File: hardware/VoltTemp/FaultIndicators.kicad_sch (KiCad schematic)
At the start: 16 parts

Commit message: layout
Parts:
- D2, D3, D4, D5, D6, D7, D8, D9: footprint LED_SMD:LED_WS2812B_PLCC4_5.0x5.0mm_P3.2mm -> LED_SMD:LED_WS2812B-2020_PLCC4_2.0x2.0mm
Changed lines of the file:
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@@
 			)
 		)
-		(property "Footprint" "LED_SMD:LED_WS2812B_PLCC4_5.0x5.0mm_P3.2mm"
+		(property "Footprint" "LED_SMD:LED_WS2812B-2020_PLCC4_2.0x2.0mm"
 			(at 120.65 60.96 0)
 			(effects
@@
 			)
 		)
-		(property "Footprint" "LED_SMD:LED_WS2812B_PLCC4_5.0x5.0mm_P3.2mm"
+		(property "Footprint" "LED_SMD:LED_WS2812B-2020_PLCC4_2.0x2.0mm"
 			(at 191.77 60.96 0)
 			(effects
@@
 			)
 		)
-		(property "Footprint" "LED_SMD:LED_WS2812B_PLCC4_5.0x5.0mm_P3.2mm"
+		(property "Footprint" "LED_SMD:LED_WS2812B-2020_PLCC4_2.0x2.0mm"
 			(at 156.21 104.14 0)
 			(effects
@@
 			)
 		)
-		(property "Footprint" "LED_SMD:LED_WS2812B_PLCC4_5.0x5.0mm_P3.2mm"
+		(property "Footprint" "LED_SMD:LED_WS2812B-2020_PLCC4_2.0x2.0mm"
 			(at 85.09 104.14 0)
 			(effects
@@
 			)
 		)
-		(property "Footprint" "LED_SMD:LED_WS2812B_PLCC4_5.0x5.0mm_P3.2mm"
+		(property "Footprint" "LED_SMD:LED_WS2812B-2020_PLCC4_2.0x2.0mm"
 			(at 85.09 60.96 0)
 			(effects
@@
 			)
 		)
-		(property "Footprint" "LED_SMD:LED_WS2812B_PLCC4_5.0x5.0mm_P3.2mm"
+		(property "Footprint" "LED_SMD:LED_WS2812B-2020_PLCC4_2.0x2.0mm"
 			(at 120.65 104.14 0)
 			(effects
@@
 			)
 		)
-		(property "Footprint" "LED_SMD:LED_WS2812B_PLCC4_5.0x5.0mm_P3.2mm"
+		(property "Footprint" "LED_SMD:LED_WS2812B-2020_PLCC4_2.0x2.0mm"
 			(at 191.77 104.14 0)
 			(effects
@@
 			)
 		)
-		(property "Footprint" "LED_SMD:LED_WS2812B_PLCC4_5.0x5.0mm_P3.2mm"
+		(property "Footprint" "LED_SMD:LED_WS2812B-2020_PLCC4_2.0x2.0mm"
 			(at 156.21 60.96 0)
 			(effects

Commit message: layout2 electric boogaloo
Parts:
- removed D2, D3, D4, D5, D6, D7, D8, D9: WS2812B, LED_SMD:LED_WS2812B-2020_PLCC4_2.0x2.0mm, symbol LED:WS2812B
- added D2, D3, D4, D5, D6, D7, D8, D9: WS2812B-2020, LED_SMD:LED_WS2812B-2020_PLCC4_2.0x2.0mm, symbol LED:WS2812B-2020
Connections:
- net +3V3: now also D2.4 (VDD), D3.4 (VDD), D4.4 (VDD), D5.4 (VDD), D6.4 (VDD), D7.4 (VDD), D8.4 (VDD), D9.4 (VDD)
- net GND: now also D2.2 (VSS), D3.2 (VSS), D4.2 (VSS), D5.2 (VSS), D6.2 (VSS), D7.2 (VSS), D8.2 (VSS), D9.2 (VSS)
- net LedDin: now also D2.3 (DIN)
- new net: D3.1 (DOUT), D4.3 (DIN)
- new net: D2.1 (DOUT), D3.3 (DIN)
- new net: D4.1 (DOUT), D5.3 (DIN)
- new net: D7.1 (DOUT), D8.3 (DIN)
- new net: D6.1 (DOUT), D7.3 (DIN)
- new net: D8.1 (DOUT), D9.3 (DIN)
- new net: D5.1 (DOUT), D6.3 (DIN)

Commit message: add thermistor test board, just need to route volttemp testpoints
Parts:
- D2, D3, D4, D5, D6, D7, D8, D9: footprint LED_SMD:LED_WS2812B-2020_PLCC4_2.0x2.0mm -> VoltTemp:WS2812B-2020
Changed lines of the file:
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@@
 			)
 		)
-		(property "Footprint" "LED_SMD:LED_WS2812B-2020_PLCC4_2.0x2.0mm"
+		(property "Footprint" "VoltTemp:WS2812B-2020"
 			(at 120.65 60.96 0)
 			(effects
@@
 			)
 		)
-		(property "Footprint" "LED_SMD:LED_WS2812B-2020_PLCC4_2.0x2.0mm"
+		(property "Footprint" "VoltTemp:WS2812B-2020"
 			(at 85.09 60.96 0)
 			(effects
@@
 			)
 		)
-		(property "Footprint" "LED_SMD:LED_WS2812B-2020_PLCC4_2.0x2.0mm"
+		(property "Footprint" "VoltTemp:WS2812B-2020"
 			(at 156.21 60.96 0)
 			(effects
@@
 			)
 		)
-		(property "Footprint" "LED_SMD:LED_WS2812B-2020_PLCC4_2.0x2.0mm"
+		(property "Footprint" "VoltTemp:WS2812B-2020"
 			(at 120.65 104.14 0)
 			(effects
@@
 			)
 		)
-		(property "Footprint" "LED_SMD:LED_WS2812B-2020_PLCC4_2.0x2.0mm"
+		(property "Footprint" "VoltTemp:WS2812B-2020"
 			(at 156.21 104.14 0)
 			(effects
@@
 			)
 		)
-		(property "Footprint" "LED_SMD:LED_WS2812B-2020_PLCC4_2.0x2.0mm"
+		(property "Footprint" "VoltTemp:WS2812B-2020"
 			(at 85.09 104.14 0)
 			(effects
@@
 			)
 		)
-		(property "Footprint" "LED_SMD:LED_WS2812B-2020_PLCC4_2.0x2.0mm"
+		(property "Footprint" "VoltTemp:WS2812B-2020"
 			(at 191.77 104.14 0)
 			(effects
@@
 			)
 		)
-		(property "Footprint" "LED_SMD:LED_WS2812B-2020_PLCC4_2.0x2.0mm"
+		(property "Footprint" "VoltTemp:WS2812B-2020"
 			(at 191.77 60.96 0)
 			(effects

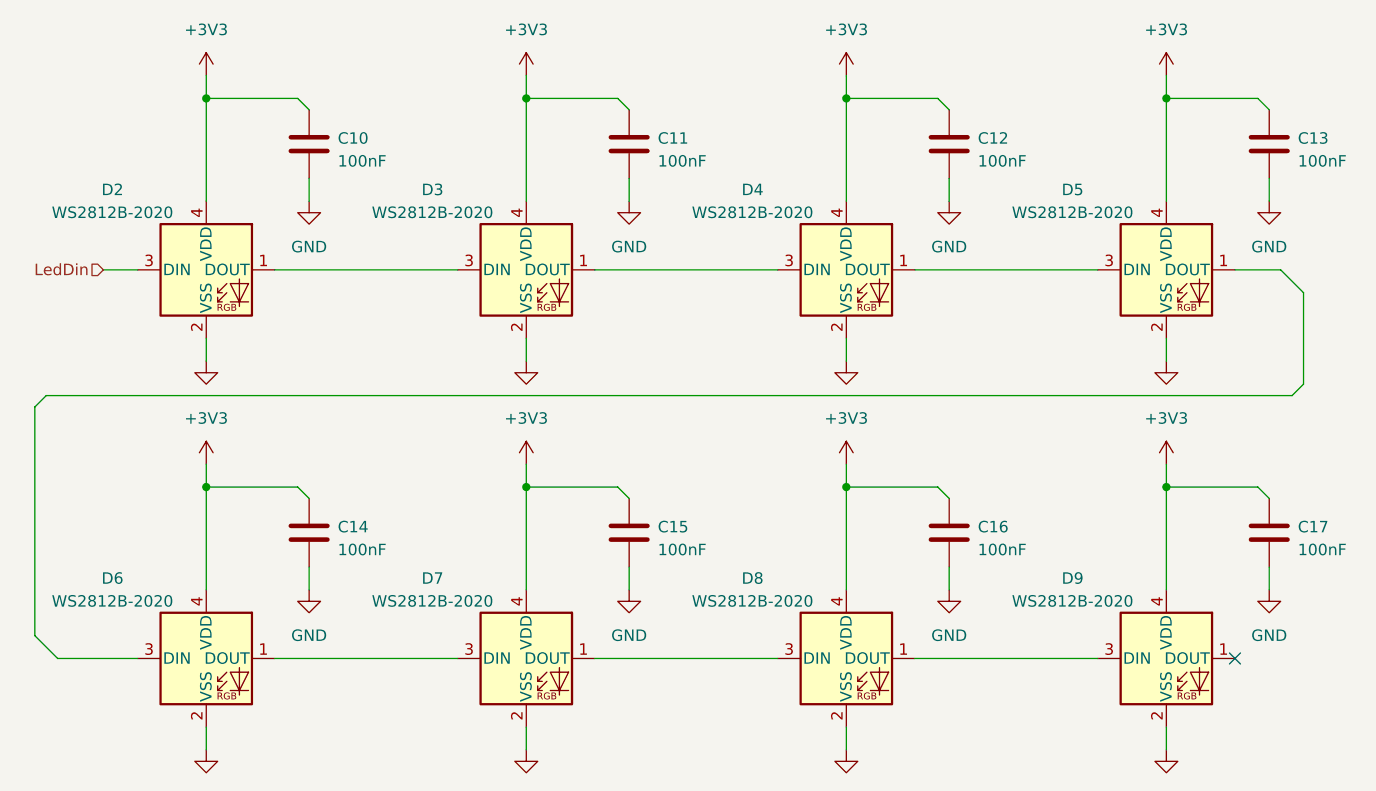
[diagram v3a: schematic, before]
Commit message: voltage testpoints
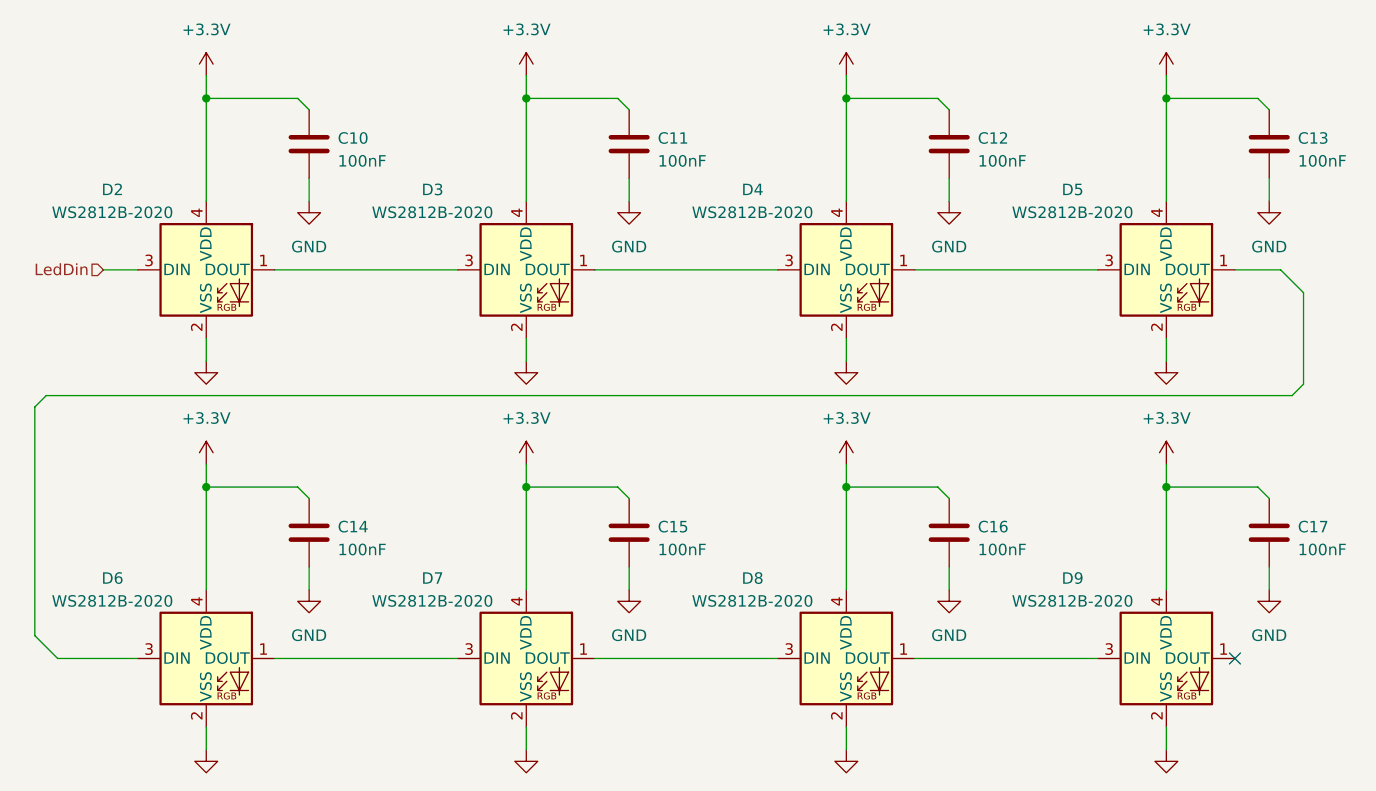
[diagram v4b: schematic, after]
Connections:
- net +3V3 renamed +3.3V

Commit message: changed bild to sharepoint
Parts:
- D2, D3, D4, D5, D6, D7, D8, D9: footprint VoltTemp:WS2812B-2020 -> LED_SMD:LED_WS2812B-2020_PLCC4_2.0x2.0mm
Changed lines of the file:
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@@
 			)
 		)
-		(property "Footprint" "VoltTemp:WS2812B-2020"
+		(property "Footprint" "LED_SMD:LED_WS2812B-2020_PLCC4_2.0x2.0mm"
 			(at 120.65 60.96 0)
 			(effects
@@
 			)
 		)
-		(property "Footprint" "VoltTemp:WS2812B-2020"
+		(property "Footprint" "LED_SMD:LED_WS2812B-2020_PLCC4_2.0x2.0mm"
 			(at 85.09 60.96 0)
 			(effects
@@
 			)
 		)
-		(property "Footprint" "VoltTemp:WS2812B-2020"
+		(property "Footprint" "LED_SMD:LED_WS2812B-2020_PLCC4_2.0x2.0mm"
 			(at 156.21 60.96 0)
 			(effects
@@
 			)
 		)
-		(property "Footprint" "VoltTemp:WS2812B-2020"
+		(property "Footprint" "LED_SMD:LED_WS2812B-2020_PLCC4_2.0x2.0mm"
 			(at 120.65 104.14 0)
 			(effects
@@
 			)
 		)
-		(property "Footprint" "VoltTemp:WS2812B-2020"
+		(property "Footprint" "LED_SMD:LED_WS2812B-2020_PLCC4_2.0x2.0mm"
 			(at 156.21 104.14 0)
 			(effects
@@
 			)
 		)
-		(property "Footprint" "VoltTemp:WS2812B-2020"
+		(property "Footprint" "LED_SMD:LED_WS2812B-2020_PLCC4_2.0x2.0mm"
 			(at 85.09 104.14 0)
 			(effects
@@
 			)
 		)
-		(property "Footprint" "VoltTemp:WS2812B-2020"
+		(property "Footprint" "LED_SMD:LED_WS2812B-2020_PLCC4_2.0x2.0mm"
 			(at 191.77 104.14 0)
 			(effects
@@
 			)
 		)
-		(property "Footprint" "VoltTemp:WS2812B-2020"
+		(property "Footprint" "LED_SMD:LED_WS2812B-2020_PLCC4_2.0x2.0mm"
 			(at 191.77 60.96 0)
 			(effects
